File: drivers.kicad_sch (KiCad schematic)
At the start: 30 parts, among them J4 MOTOR1, J5 MOTOR2, U6 MC33926PNB, U7 MC33926PNB

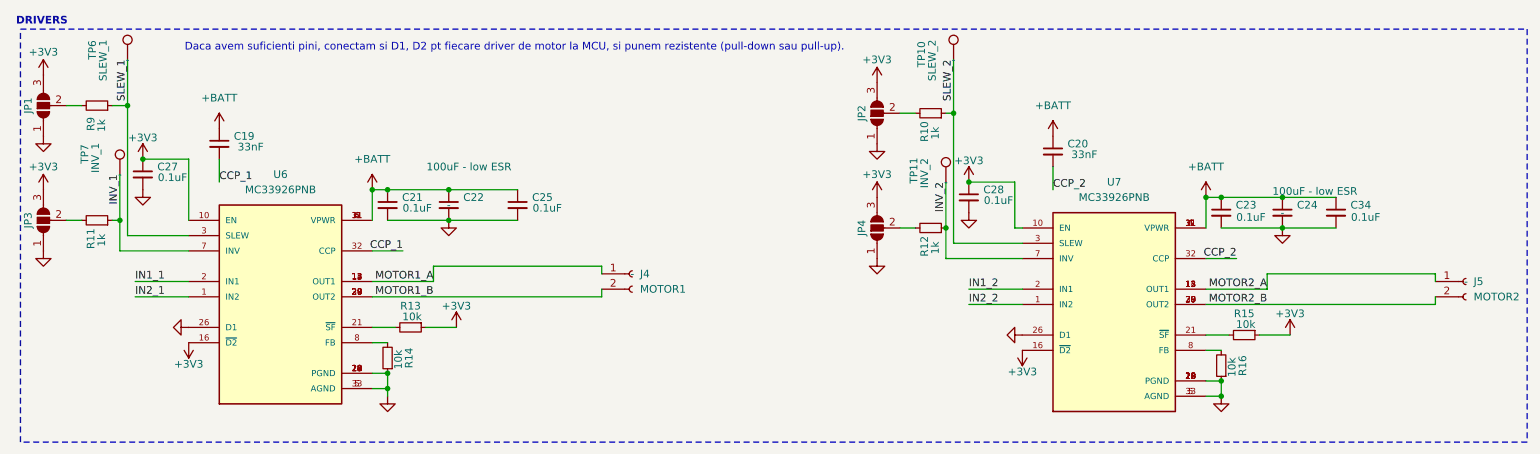
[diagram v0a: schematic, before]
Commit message: added global labels
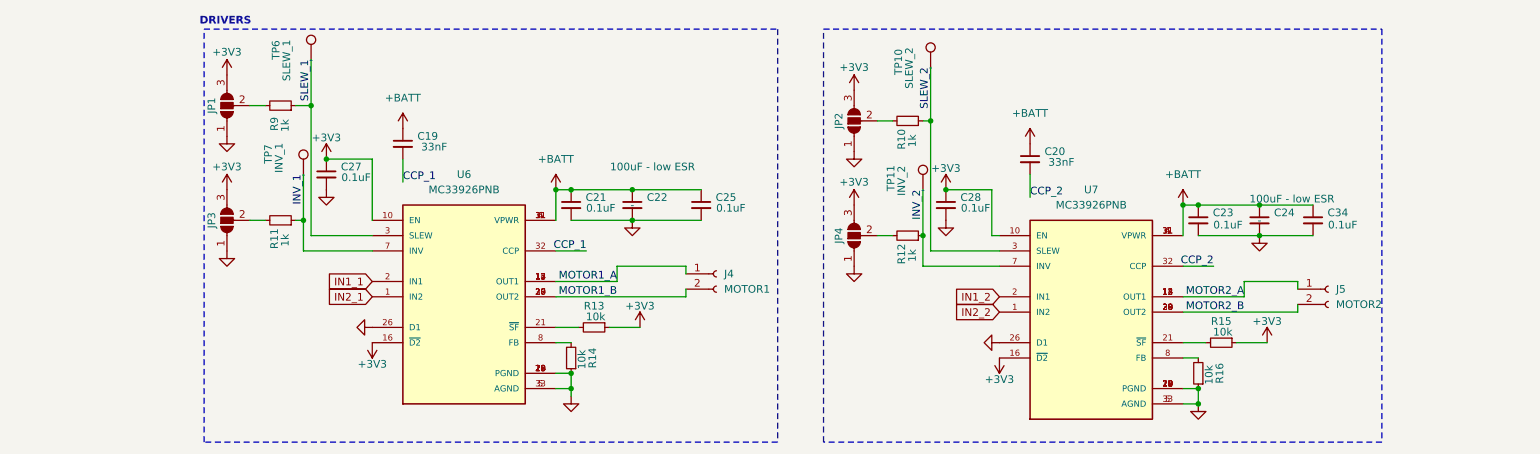
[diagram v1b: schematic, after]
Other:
- note removed: "Daca avem suficienti pini, conectam si D1, D2 pt fiecare driver de motor la MCU, si punem rezistente (pull-down sau pull-up)."
- moved on the sheet: C19, C20, C21, C22, C23, C24, C25, C27, C28, C34, J4, J5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

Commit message: added PDFs
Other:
- title: (none) -> Minisumo PCB
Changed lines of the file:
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@@
 	(generator_version "9.0")
 	(paper "A4")
+	(title_block
+		(title "Minisumo PCB")
+		(date "2025-04-16")
+		(rev "3.2")
+		(comment 2 "alex_ivan1304@outlook.com")
+		(comment 3 "Designed by: Ivan Alexandru Marian")
+	)
 	(rectangle
 		(start 157.48 64.77)

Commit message: custom
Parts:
- added C37, C38: 0.1uF, Capacitor_SMD:C_0603_1608Metric, symbol Device:C_Small
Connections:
- net +BATT: now also C37.1, C38.1
- net GND: now also C37.2, C38.2
